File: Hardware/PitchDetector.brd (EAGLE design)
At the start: 81.3 x 93.2 mm, 46 parts, among them IC1 STM32F302CBT6, IC2 LM3940IMP-3.3_NOPB, X1 MINI-USB-32005-201, X2 HD44780LCD-1602, Y1 ABLS-8.000MHZ-K4T

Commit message: PCB updated.
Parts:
- moved TM1 60.7 mm to (111.4, 5.10)
- moved C5 49.9 mm to (91.9, 70.4)
- moved R6 48.9 mm to (91.9, 75.2)
- moved C14 38.8 mm to (105.5, 5.11)
- moved LED3 38.0 mm to (71.3, 12.2), turned to 0 degrees
- moved LED2 36.7 mm to (71.3, 18.5), turned to 0 degrees
- moved C12 36.7 mm to (105.5, 16.1)
- moved C11 36.6 mm to (87.7, 16.2)
- moved C10 36.6 mm to (87.6, 5.26)
- moved C13 36.5 mm to (87.6, 10.8)
- moved X1 36.4 mm to (96.1, 7.33)
- moved IC2 35.7 mm to (96.2, 20.6), turned to 90 degrees
- moved C1 35.7 mm to (105.5, 10.7), turned to 270 degrees
- moved LED1 35.3 mm to (71.3, 24.9), turned to 180 degrees
- moved R7 32.0 mm to (105.5, 50.7), turned to 90 degrees
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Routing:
- net 3V3: track 213.2 -> 278.6 mm, vias 5 -> 2
- net N$10: track 16.7 -> 73.4 mm, vias 0 -> 1
- net CGND: track 156.6 -> 108.0 mm, vias 2 -> 4
- net IN-: track 66.3 -> 18.1 mm, vias 3 -> 0
- net ADC0: track 81.8 -> 42.4 mm, vias 2 -> 0
- net N$9: track 12.4 -> 50.7 mm
- net XTAL1: track 50.8 -> 20.6 mm, vias 0 -> 2
- net GND: track 339.7 -> 317.1 mm, vias 8 -> 0
- net SWO: track 38.9 -> 61.2 mm, vias 0 -> 1
- net VUSB: track 24.4 -> 46.1 mm, vias 0 -> 3
- net N$6: track 10.9 -> 30.5 mm
- net N$1: track 28.2 -> 46.6 mm
- net LCD_RS: track 35.8 -> 54.1 mm, vias 2 -> 1
- net N$11: track 40.5 -> 56.5 mm, vias 0 -> 2
- net LCD_D6: track 33.2 -> 17.5 mm
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- added copper zone on layer 1, net GND
- added copper zone on layer 16, net GND
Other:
- board size 81.3 x 93.2 mm -> 59.6 x 92.8 mm
- board text added: "Pitch Detector - Designed by Group PE04"
- board text removed: "Designed by Group PE04"
- board text removed: "Pitch Detector"

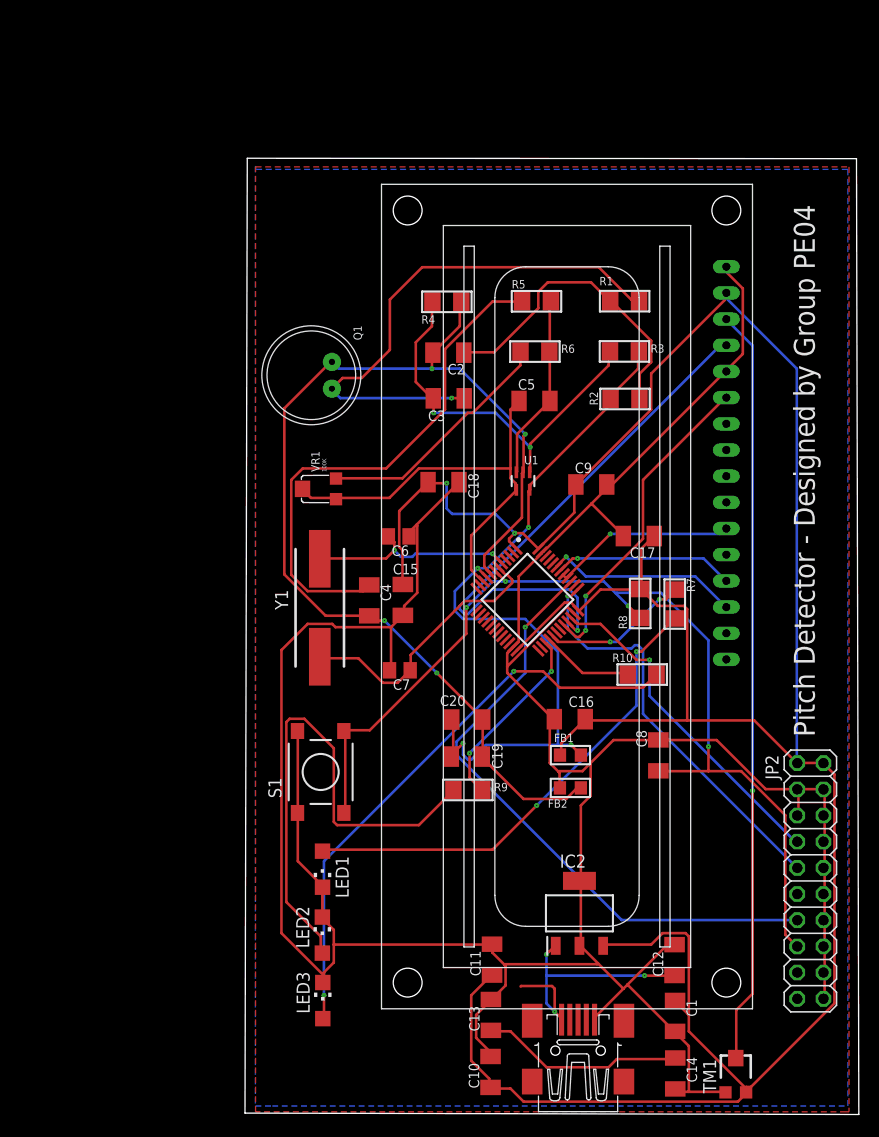
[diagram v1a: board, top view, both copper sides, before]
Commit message: Schematic bug fix. PCB updated.
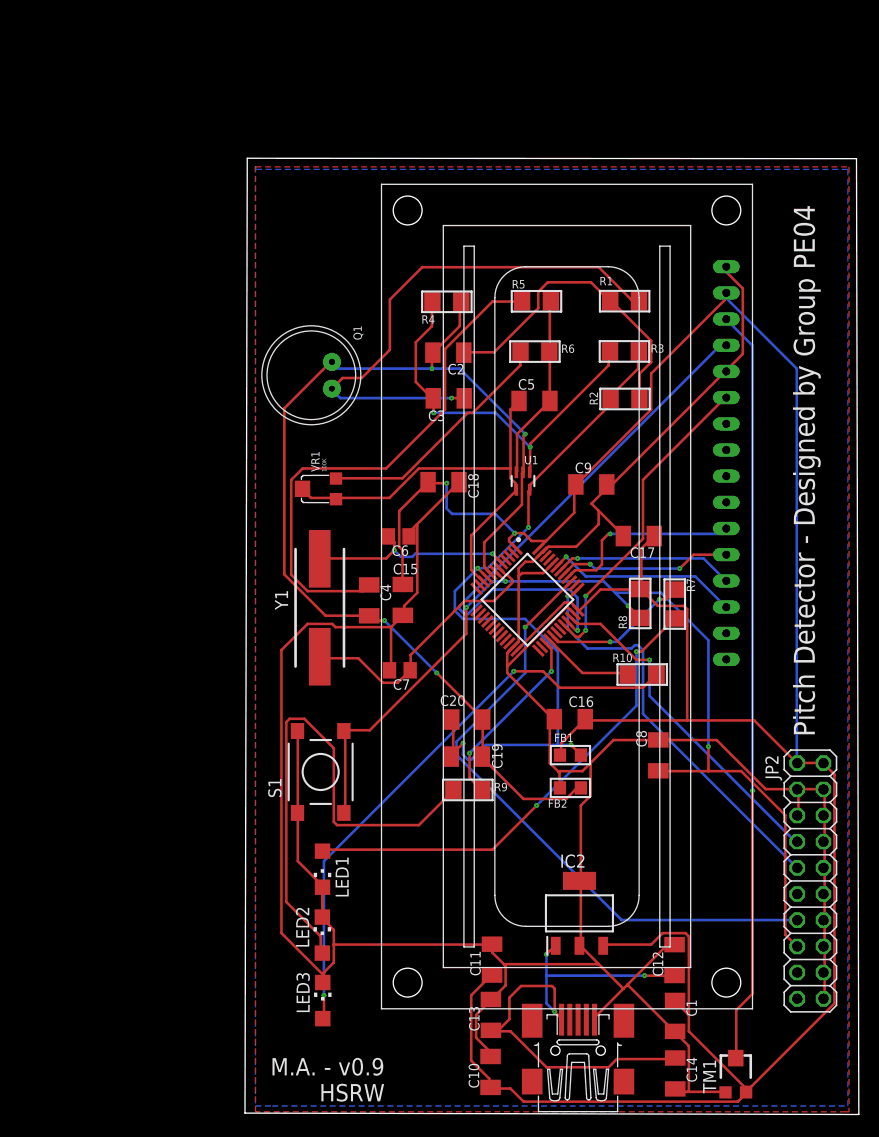
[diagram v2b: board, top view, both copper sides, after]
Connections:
- net GND: now also IC1.44
- net LCD_D4: no longer IC1.41
- net LCD_D5: now also IC1.41
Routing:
- net LCD_D5: track 0.00 -> 16.9 mm, vias 0 -> 2
- net VUSB: track 46.1 -> 51.9 mm
- net GND: track 317.1 -> 322.5 mm
- net LCD_D4: track 18.1 -> 18.8 mm
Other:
- board text added: "M.A. - v0.9 HSRW"

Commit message: Stable board and schematic added.
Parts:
- turned C9 to 180 degrees
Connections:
- net 3V3: now also X2.15
- net GND: now also X2.16
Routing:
- net CGND: track 108.0 -> 143.5 mm, vias 4 -> 2
- net N$12: track 50.2 -> 31.3 mm
- net LCD_RS: track 54.1 -> 37.1 mm, vias 1 -> 3
- net VUSB: track 51.9 -> 38.0 mm
- net N$10: track 73.4 -> 84.4 mm, vias 1 -> 0
- net 3V3: track 279.0 -> 289.6 mm, vias 2 -> 4
- net SWDIO: track 33.1 -> 42.9 mm
- net N$11: track 56.5 -> 46.9 mm
- net C3V3: track 74.6 -> 66.0 mm
- net SWO: track 61.2 -> 53.5 mm
- net NRST: track 98.2 -> 92.4 mm
- net LCD_D7: track 18.9 -> 24.4 mm
- net N$5: track 52.2 -> 48.8 mm
- net N$1: track 46.6 -> 49.5 mm
- net LCD_EN: track 31.2 -> 33.7 mm, vias 2 -> 0
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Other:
- board text added: "M.A. - v1.0 HSRW"
- board text removed: "M.A. - v0.9 HSRW"
